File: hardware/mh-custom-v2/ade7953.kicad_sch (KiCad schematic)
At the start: 59 parts, among them U2 ADE7953xCP, Y1 3.58MHz

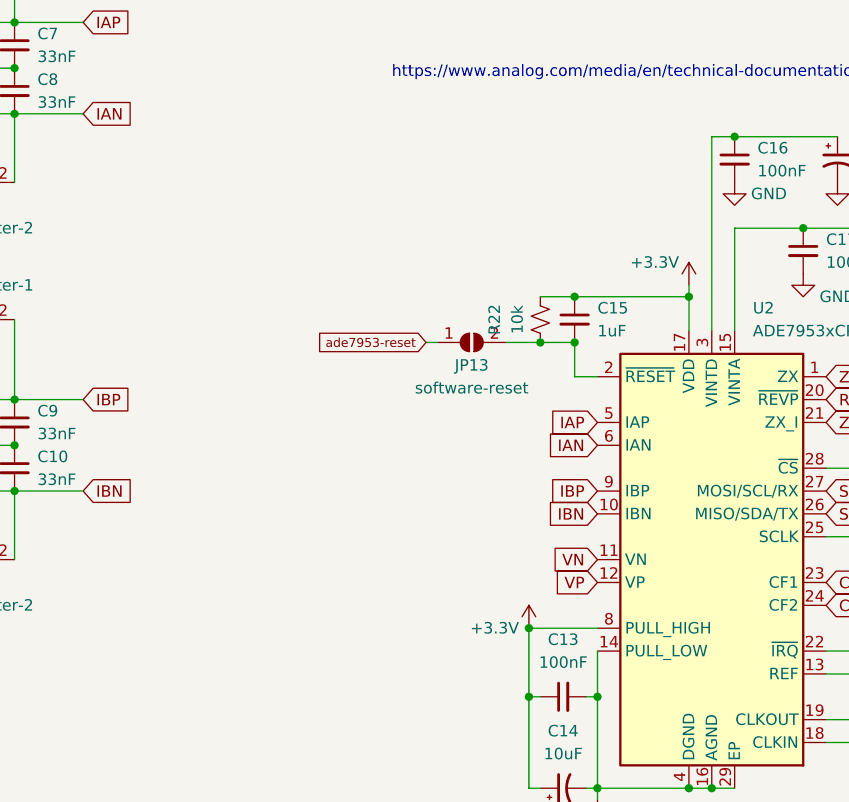
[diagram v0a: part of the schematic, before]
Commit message: b-silkscreen fixed
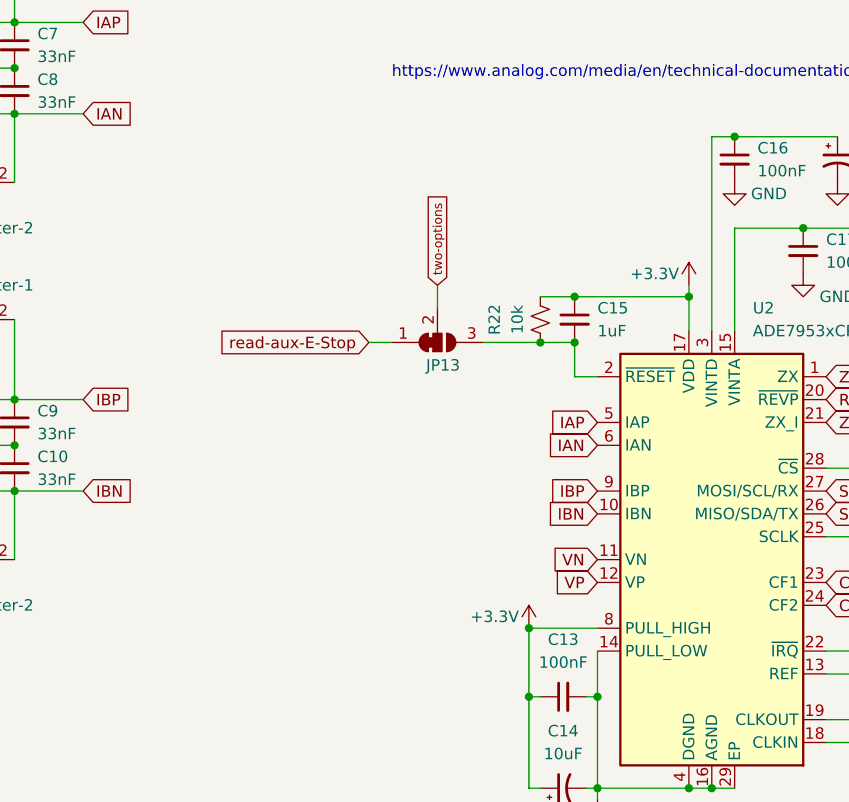
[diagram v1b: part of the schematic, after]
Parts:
- removed JP13: software-reset, Jumper:SolderJumper-2_P1.3mm_Open_RoundedPad1.0x1.5mm, symbol Jumper:SolderJumper_2_Open
- added JP13: SolderJumper_3_Bridged12, Jumper:SolderJumper-3_P1.3mm_Bridged12_RoundedPad1.0x1.5mm, symbol Jumper:SolderJumper_3_Bridged12
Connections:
- net at C15.2, R22.1, U2.2 (~{RESET}): now also JP13.3 (B)
- net +3V3 renamed +3.3V
- new net read-aux-E-Stop: JP13.1 (A)
- new net two-options: JP13.2 (C)
